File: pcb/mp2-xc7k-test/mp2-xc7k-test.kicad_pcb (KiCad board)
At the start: 4 copper layers, 0 parts

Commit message: Continued layout, 454 unrouted
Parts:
- added C1: 10 uF, azonenberg_pcb:EIA_1210_CAP_NOSILK, F.Cu at (95.0, 66.5)
- added C10: 0.47 uF, azonenberg_pcb:EIA_0402_CAP_NOSILK, F.Cu at (93.8, 99.2)
- added C100: 1 uF, azonenberg_pcb:EIA_0201_CAP_NOSILK, B.Cu at (200.0, 87.1)
- added C101: 1 uF, azonenberg_pcb:EIA_0201_CAP_NOSILK, B.Cu at (208.7, 92.0)
- added C102: 1 uF, azonenberg_pcb:EIA_0201_CAP_NOSILK, B.Cu at (205.6, 85.5)
- added C103: 1 uF, azonenberg_pcb:EIA_0201_CAP_NOSILK, B.Cu at (204.8, 83.3)
- added C104: 1 uF, azonenberg_pcb:EIA_0201_CAP_NOSILK, B.Cu at (199.2, 83.9)
- added C105: 1 uF, azonenberg_pcb:EIA_0201_CAP_NOSILK, B.Cu at (204.8, 84.7)
- added C106: 1 uF, azonenberg_pcb:EIA_0201_CAP_NOSILK, B.Cu at (201.5, 83.2)
- added C107: 1 uF, azonenberg_pcb:EIA_0201_CAP_NOSILK, B.Cu at (204.0, 85.5)
- added C108: 1 uF, azonenberg_pcb:EIA_0201_CAP_NOSILK, B.Cu at (199.2, 83.1)
- added C109: 1 uF, azonenberg_pcb:EIA_0201_CAP_NOSILK, B.Cu at (200.8, 85.5)
- added C11: DNP, azonenberg_pcb:EIA_0402_CAP_NOSILK, F.Cu at (93.8, 100.7)
- added C110: 1 uF, azonenberg_pcb:EIA_0201_CAP_NOSILK, B.Cu at (208.7, 91.2)
- added C111: 1 uF, azonenberg_pcb:EIA_0201_CAP_NOSILK, B.Cu at (207.2, 91.3)
- added C112: 1 uF, azonenberg_pcb:EIA_0201_CAP_NOSILK, B.Cu at (197.7, 80.8)
- added C113: 1 uF, azonenberg_pcb:EIA_0201_CAP_NOSILK, B.Cu at (197.6, 82.3)
- added C114: 1 uF, azonenberg_pcb:EIA_0201_CAP_NOSILK, B.Cu at (197.6, 83.0)
- added C115: 0.47 uF, azonenberg_pcb:EIA_0402_CAP_NOSILK, F.Cu at (98.8, 93.2)
- added C116: 0.47 uF, azonenberg_pcb:EIA_0402_CAP_NOSILK, F.Cu at (98.8, 94.7)
- added C117: 4.7 uF, azonenberg_pcb:EIA_0603_CAP_NOSILK, B.Cu at (197.2, 85.2)
- added C118: 1 uF, azonenberg_pcb:EIA_0201_CAP_NOSILK, B.Cu at (200.1, 80.8)
- added C119: 1 uF, azonenberg_pcb:EIA_0201_CAP_NOSILK, B.Cu at (200.1, 82.4)
- added C12: 22 uF, azonenberg_pcb:EIA_1210_CAP_NOSILK, F.Cu at (95.0, 70.4)
- added C120: 1 uF, azonenberg_pcb:EIA_0201_CAP_NOSILK, B.Cu at (198.5, 82.4)
- added C121: 1 uF, azonenberg_pcb:EIA_0201_CAP_NOSILK, B.Cu at (199.4, 80.8)
- added C122: 1 uF, azonenberg_pcb:EIA_0201_CAP_NOSILK, B.Cu at (198.5, 80.8)
- added C123: 4.7 uF, azonenberg_pcb:EIA_0603_CAP_NOSILK, B.Cu at (199.4, 91.6)
- added C124: DNP, azonenberg_pcb:EIA_0402_CAP_NOSILK, F.Cu at (98.8, 96.2)
- added C125: 4.7 uF, azonenberg_pcb:EIA_0603_CAP_NOSILK, F.Cu at (170.6, 147.0)
- added C126: 0.47 uF, azonenberg_pcb:EIA_0402_CAP_NOSILK, F.Cu at (144.7, 142.8)
- added C127: 0.47 uF, azonenberg_pcb:EIA_0402_CAP_NOSILK, F.Cu at (144.7, 144.3)
- added C128: 1 uF, azonenberg_pcb:EIA_0201_CAP_NOSILK, B.Cu at (197.6, 91.3)
- added C129: 22 uF, azonenberg_pcb:EIA_1210_CAP_NOSILK, F.Cu at (105.0, 66.5)
- added C13: 4.7 uF, azonenberg_pcb:EIA_0603_CAP_NOSILK, F.Cu at (88.8, 107.2)
- added C130: 0.47 uF, azonenberg_pcb:EIA_0402_CAP_NOSILK, F.Cu at (98.8, 97.7)
- added C131: 0.47 uF, azonenberg_pcb:EIA_0402_CAP_NOSILK, B.Cu at (196.8, 128.5)
- added C132: 0.47 uF, azonenberg_pcb:EIA_0402_CAP_NOSILK, B.Cu at (204.6, 103.2)
- added C133: 0.1 uF, azonenberg_pcb:EIA_0402_CAP_NOSILK, F.Cu at (205.2, 101.2)
- added C134: 0.1 uF, azonenberg_pcb:EIA_0402_CAP_NOSILK, F.Cu at (206.1, 101.2)
- added C135: 0.47 uF, azonenberg_pcb:EIA_0402_CAP_NOSILK, B.Cu at (201.6, 64.2)
- added C136: 4.7 uF, azonenberg_pcb:EIA_0603_CAP_NOSILK, F.Cu at (191.5, 63.2)
- added C137: 0.47 uF, azonenberg_pcb:EIA_0402_CAP_NOSILK, B.Cu at (195.1, 67.5)
- added C138: 0.47 uF, azonenberg_pcb:EIA_0402_CAP_NOSILK, B.Cu at (194.0, 63.6)
- added C139: 0.47 uF, azonenberg_pcb:EIA_0402_CAP_NOSILK, B.Cu at (199.0, 66.0)
- added C14: 4.7 uF, azonenberg_pcb:EIA_0603_CAP_NOSILK, F.Cu at (88.8, 109.0)
- added C140: 1 uF, azonenberg_pcb:EIA_0201_CAP_NOSILK, B.Cu at (198.3, 90.4)
- added C15: DNP, azonenberg_pcb:EIA_0402_CAP_NOSILK, F.Cu at (96.3, 88.7)
- added C16: 22 uF, azonenberg_pcb:EIA_1210_CAP_NOSILK, F.Cu at (95.0, 74.3)
- added C17: 0.47 uF, azonenberg_pcb:EIA_0402_CAP_NOSILK, F.Cu at (96.3, 90.2)
- added C18: 4.7 uF, azonenberg_pcb:EIA_0603_CAP_NOSILK, F.Cu at (88.8, 110.8)
- added C19: 4.7 uF, azonenberg_pcb:EIA_0603_CAP_NOSILK, F.Cu at (88.8, 112.7)
- added C2: 0.47 uF, azonenberg_pcb:EIA_0402_CAP_NOSILK, F.Cu at (93.8, 88.7)
- added C20: DNP, azonenberg_pcb:EIA_0402_CAP_NOSILK, F.Cu at (96.3, 91.7)
- added C21: 22 uF, azonenberg_pcb:EIA_1210_CAP_NOSILK, F.Cu at (95.0, 78.2)
- added C22: 0.47 uF, azonenberg_pcb:EIA_0402_CAP_NOSILK, F.Cu at (96.3, 93.2)
- added C23: 0.47 uF, azonenberg_pcb:EIA_0402_CAP_NOSILK, F.Cu at (96.3, 94.7)
- added C24: 10 uF, azonenberg_pcb:EIA_1210_CAP_NOSILK, F.Cu at (95.0, 82.1)
- added C25: 47 uF, azonenberg_pcb:EIA_1206_CAP_NOSILK, F.Cu at (112.5, 89.2)
- added C26: 47 uF, azonenberg_pcb:EIA_1206_CAP_NOSILK, F.Cu at (112.5, 91.8)
- added C267: 1 uF, azonenberg_pcb:EIA_0201_CAP_NOSILK, B.Cu at (196.9, 81.6)
- added C268: 1 uF, azonenberg_pcb:EIA_0201_CAP_NOSILK, B.Cu at (197.7, 78.4)
- added C269: 1 uF, azonenberg_pcb:EIA_0201_CAP_NOSILK, B.Cu at (206.3, 83.2)
- added C27: 0.47 uF, azonenberg_pcb:EIA_0402_CAP_NOSILK, F.Cu at (96.3, 96.2)
- added C270: 1 uF, azonenberg_pcb:EIA_0201_CAP_NOSILK, B.Cu at (207.2, 92.1)
- added C271: 1 uF, azonenberg_pcb:EIA_0201_CAP_NOSILK, B.Cu at (195.2, 78.5)
- added C272: 1 uF, azonenberg_pcb:EIA_0201_CAP_NOSILK, B.Cu at (207.2, 81.7)
- added C273: 1 uF, azonenberg_pcb:EIA_0201_CAP_NOSILK, B.Cu at (198.4, 84.6)
- added C274: 1 uF, azonenberg_pcb:EIA_0201_CAP_NOSILK, B.Cu at (199.2, 84.9)
- added C28: 10 uF, azonenberg_pcb:EIA_1210_CAP_NOSILK, F.Cu at (95.0, 86.0)
- added C29: 0.47 uF, azonenberg_pcb:EIA_0402_CAP_NOSILK, F.Cu at (96.3, 97.7)
- added C3: 4.7 uF, azonenberg_pcb:EIA_0603_CAP_NOSILK, F.Cu at (88.8, 105.5)
- added C30: 0.47 uF, azonenberg_pcb:EIA_0402_CAP_NOSILK, F.Cu at (96.3, 99.2)
- added C31: 10 uF, azonenberg_pcb:EIA_1210_CAP_NOSILK, F.Cu at (100.0, 66.5)
- added C32: 10 uF, azonenberg_pcb:EIA_1210_CAP_NOSILK, F.Cu at (100.0, 70.4)
- added C33: 22 uF, azonenberg_pcb:EIA_1206_CAP_NOSILK, F.Cu at (112.5, 94.4)
- added C34: 0.47 uF, azonenberg_pcb:EIA_0402_CAP_NOSILK, F.Cu at (96.3, 100.7)
- added C35: 10 uF, azonenberg_pcb:EIA_1210_CAP_NOSILK, F.Cu at (100.0, 74.3)
- added C36: 22 uF, azonenberg_pcb:EIA_1206_CAP_NOSILK, F.Cu at (112.5, 97.0)
- added C37: 0.47 uF, azonenberg_pcb:EIA_0402_CAP_NOSILK, F.Cu at (98.8, 88.7)
- added C38: 10 uF, azonenberg_pcb:EIA_1210_CAP_NOSILK, F.Cu at (100.0, 78.2)
- added C39: 47 uF, azonenberg_pcb:EIA_1206_CAP_NOSILK, F.Cu at (112.5, 99.6)
- added C4: 0.1 uF, azonenberg_pcb:EIA_0402_CAP_NOSILK, F.Cu at (93.8, 90.2)
- added C40: 0.47 uF, azonenberg_pcb:EIA_0402_CAP_NOSILK, F.Cu at (98.8, 90.2)
- added C41: 10 uF, azonenberg_pcb:EIA_1210_CAP_NOSILK, F.Cu at (100.0, 82.1)
- added C42: 0.47 uF, azonenberg_pcb:EIA_0402_CAP_NOSILK, F.Cu at (174.5, 149.5)
- added C43: 330 uF, azonenberg_pcb:EIA_1210_CAP_NOSILK, F.Cu at (127.8, 132.7)
- added C44: 0.22 uF, azonenberg_pcb:EIA_0402_CAP_NOSILK, F.Cu at (199.8, 107.0)
- added C45: 0.22 uF, azonenberg_pcb:EIA_0402_CAP_NOSILK, F.Cu at (199.8, 107.8)
- added C46: 0.22 uF, azonenberg_pcb:EIA_0402_CAP_NOSILK, F.Cu at (204.4, 109.6)
- added C47: 0.22 uF, azonenberg_pcb:EIA_0402_CAP_NOSILK, F.Cu at (204.4, 108.8)
- added C48: 22 uF, azonenberg_pcb:EIA_0805_CAP_NOSILK, F.Cu at (167.1, 143.2)
- added C49: 330 uF, azonenberg_pcb:EIA_1210_CAP_NOSILK, F.Cu at (127.8, 136.6)
- added C5: 0.47 uF, azonenberg_pcb:EIA_0402_CAP_NOSILK, F.Cu at (93.8, 91.7)
- added C50: 0.1 uF, azonenberg_pcb:EIA_0402_CAP_NOSILK, F.Cu at (142.2, 142.8)
- added C51: 0.1 uF, azonenberg_pcb:EIA_0402_CAP_NOSILK, F.Cu at (142.2, 144.3)
- added C52: 0.1 uF, azonenberg_pcb:EIA_0402_CAP_NOSILK, F.Cu at (199.8, 112.0)
- added C53: 0.1 uF, azonenberg_pcb:EIA_0402_CAP_NOSILK, F.Cu at (142.2, 147.3)
- added C54: 0.1 uF, azonenberg_pcb:EIA_0402_CAP_NOSILK, F.Cu at (144.7, 135.3)
- added C55: 22 uF, azonenberg_pcb:EIA_0805_CAP_NOSILK, F.Cu at (167.1, 145.8)
- added C56: 100 uF, azonenberg_pcb:EIA_1210_CAP_NOSILK, F.Cu at (127.8, 140.5)
- added C57: 4.7 uF, azonenberg_pcb:EIA_0603_CAP_NOSILK, F.Cu at (131.9, 131.7)
- added C58: 4.7 uF, azonenberg_pcb:EIA_0603_CAP_NOSILK, B.Cu at (175.0, 82.5)
- added C59: 4.7 uF, azonenberg_pcb:EIA_0603_CAP_NOSILK, B.Cu at (166.0, 82.5)
- added C6: 0.47 uF, azonenberg_pcb:EIA_0402_CAP_NOSILK, F.Cu at (93.8, 93.2)
- added C60: 47 uF, azonenberg_pcb:EIA_1210_CAP_NOSILK, F.Cu at (177.0, 98.4)
- added C61: 47 uF, azonenberg_pcb:EIA_1210_CAP_NOSILK, F.Cu at (177.0, 101.6)
- added C62: 47 uF, azonenberg_pcb:EIA_1210_CAP_NOSILK, F.Cu at (180.2, 104.8)
- added C63: 47 uF, azonenberg_pcb:EIA_1210_CAP_NOSILK, F.Cu at (121.2, 141.7)
- added C64: 4.7 uF, azonenberg_pcb:EIA_0603_CAP_NOSILK, F.Cu at (131.9, 137.1)
- added C65: 4.7 uF, azonenberg_pcb:EIA_0603_CAP_NOSILK, F.Cu at (131.9, 138.9)
- added C66: 4.7 uF, azonenberg_pcb:EIA_0603_CAP_NOSILK, F.Cu at (131.9, 140.7)
- added C67: 0.1 uF, azonenberg_pcb:EIA_0402_CAP_NOSILK, F.Cu at (199.8, 111.2)
- added C68: 0.47 uF, azonenberg_pcb:EIA_0402_CAP_NOSILK, B.Cu at (188.2, 93.0)
- added C69: 1 uF, azonenberg_pcb:EIA_0201_CAP_NOSILK, B.Cu at (200.8, 89.5)
- added C7: 0.47 uF, azonenberg_pcb:EIA_0402_CAP_NOSILK, F.Cu at (93.8, 94.7)
- added C70: 1 uF, azonenberg_pcb:EIA_0201_CAP_NOSILK, B.Cu at (200.8, 87.9)
- added C71: 1 uF, azonenberg_pcb:EIA_0201_CAP_NOSILK, B.Cu at (204.8, 89.5)
- added C72: 1 uF, azonenberg_pcb:EIA_0201_CAP_NOSILK, B.Cu at (203.2, 84.9)
- added C73: 1 uF, azonenberg_pcb:EIA_0201_CAP_NOSILK, B.Cu at (196.1, 80.0)
- added C74: 1 uF, azonenberg_pcb:EIA_0201_CAP_NOSILK, B.Cu at (200.8, 88.7)
- added C75: 0.47 uF, azonenberg_pcb:EIA_0402_CAP_NOSILK, F.Cu at (144.7, 138.3)
- added C76: 0.1 uF, azonenberg_pcb:EIA_0402_CAP_NOSILK, F.Cu at (144.7, 139.8)
- added C77: 0.1 uF, azonenberg_pcb:EIA_0402_CAP_NOSILK, F.Cu at (144.7, 141.3)
- added C78: 1 uF, azonenberg_pcb:EIA_0201_CAP_NOSILK, B.Cu at (203.2, 87.9)
- added C79: 1 uF, azonenberg_pcb:EIA_0201_CAP_NOSILK, B.Cu at (206.3, 89.6)
- added C8: 0.47 uF, azonenberg_pcb:EIA_0402_CAP_NOSILK, F.Cu at (93.8, 96.2)
- added C80: 1 uF, azonenberg_pcb:EIA_0201_CAP_NOSILK, B.Cu at (203.2, 84.1)
- added C81: 1 uF, azonenberg_pcb:EIA_0201_CAP_NOSILK, B.Cu at (200.8, 87.1)
- added C82: 1 uF, azonenberg_pcb:EIA_0201_CAP_NOSILK, B.Cu at (199.2, 89.5)
- added C83: 1 uF, azonenberg_pcb:EIA_0201_CAP_NOSILK, B.Cu at (203.2, 87.1)
- added C84: 1 uF, azonenberg_pcb:EIA_0201_CAP_NOSILK, B.Cu at (204.8, 88.7)
- added C85: 1 uF, azonenberg_pcb:EIA_0201_CAP_NOSILK, B.Cu at (203.2, 83.3)
- added C86: 1 uF, azonenberg_pcb:EIA_0201_CAP_NOSILK, B.Cu at (200.8, 84.7)
- added C87: 1 uF, azonenberg_pcb:EIA_0201_CAP_NOSILK, B.Cu at (199.2, 88.7)
- added C88: 1 uF, azonenberg_pcb:EIA_0201_CAP_NOSILK, B.Cu at (203.2, 88.7)
- added C89: 1 uF, azonenberg_pcb:EIA_0201_CAP_NOSILK, B.Cu at (204.8, 87.9)
- added C9: 0.47 uF, azonenberg_pcb:EIA_0402_CAP_NOSILK, F.Cu at (93.8, 97.7)
- added C90: 1 uF, azonenberg_pcb:EIA_0201_CAP_NOSILK, B.Cu at (203.2, 82.5)
- added C91: 1 uF, azonenberg_pcb:EIA_0201_CAP_NOSILK, B.Cu at (200.8, 83.9)
- added C92: 1 uF, azonenberg_pcb:EIA_0201_CAP_NOSILK, B.Cu at (199.2, 87.9)
- added C93: 1 uF, azonenberg_pcb:EIA_0201_CAP_NOSILK, B.Cu at (203.2, 89.5)
- added C94: 1 uF, azonenberg_pcb:EIA_0201_CAP_NOSILK, B.Cu at (204.8, 87.1)
- added C95: 22 uF, azonenberg_pcb:EIA_1206_CAP_NOSILK, F.Cu at (112.5, 102.2)
- added C96: 10 uF, azonenberg_pcb:EIA_1210_CAP_NOSILK, F.Cu at (100.0, 86.0)
- added C97: 0.47 uF, azonenberg_pcb:EIA_0402_CAP_NOSILK, F.Cu at (98.8, 91.7)
- added C98: 1 uF, azonenberg_pcb:EIA_0201_CAP_NOSILK, B.Cu at (204.8, 82.5)
- added C99: 1 uF, azonenberg_pcb:EIA_0201_CAP_NOSILK, B.Cu at (200.0, 84.7)
- added D1: GREEN, azonenberg_pcb:EIA_0402_LED, F.Cu at (98.8, 99.2)
- added D10: GREEN, azonenberg_pcb:EIA_0402_LED, F.Cu at (189.8, 82.8)
- added D11: GREEN, azonenberg_pcb:EIA_0402_LED, F.Cu at (190.5, 82.8)
- added D12: RED, azonenberg_pcb:EIA_0402_LED, F.Cu at (199.4, 122.0)
- added D2: GREEN, azonenberg_pcb:EIA_0402_LED, F.Cu at (98.8, 100.7)
- added D3: RED, azonenberg_pcb:EIA_0402_LED, F.Cu at (101.3, 88.7)
- added D31: GREEN, azonenberg_pcb:EIA_0402_LED, F.Cu at (154.2, 149.0)
- added D32: GREEN, azonenberg_pcb:EIA_0402_LED, F.Cu at (167.4, 133.8)
- added D33: GREEN, azonenberg_pcb:EIA_0402_LED, F.Cu at (167.4, 135.6)
- added D34: GREEN, azonenberg_pcb:EIA_0402_LED, F.Cu at (167.4, 137.3)
- added D39: GREEN, azonenberg_pcb:EIA_0402_LED, F.Cu at (167.4, 139.2)
- added D4: GREEN, azonenberg_pcb:EIA_0402_LED, F.Cu at (188.2, 79.5)
- added D40: GREEN, azonenberg_pcb:EIA_0402_LED, F.Cu at (167.4, 140.9)
- added D5: GREEN, azonenberg_pcb:EIA_0402_LED, F.Cu at (189.0, 79.5)
- added D6: GREEN, azonenberg_pcb:EIA_0402_LED, F.Cu at (189.8, 79.5)
- added D7: GREEN, azonenberg_pcb:EIA_0402_LED, F.Cu at (190.5, 79.5)
- added D8: GREEN, azonenberg_pcb:EIA_0402_LED, F.Cu at (188.2, 82.8)
- added D9: GREEN, azonenberg_pcb:EIA_0402_LED, F.Cu at (189.0, 82.8)
- added F1: 3A, azonenberg_pcb:EIA_0402_RES_NOSILK, F.Cu at (101.3, 90.2)
- added FB1: MI0603J601R-10, azonenberg_pcb:EIA_0603_INDUCTOR_NOSILK, F.Cu at (88.8, 114.5)
- added FB7: MI0603J601R-10, azonenberg_pcb:EIA_0603_INDUCTOR_NOSILK, B.Cu at (187.6, 90.6)
- added FB8: MI0603J601R-10, azonenberg_pcb:EIA_0603_INDUCTOR_NOSILK, B.Cu at (187.6, 91.6)
- added J1: BARREL_JACK, azonenberg_pcb:CONN_CUI_PJ-058BH_HIPWR_BARREL_NOSLOT, F.Cu at (131.5, 68.5)
- added J10: SMPM, azonenberg_pcb:CONN_SMPM_AMPHENOL_C925-197J-51PT, F.Cu at (196.0, 101.8)
- added J12: PMOD_HOST, azonenberg_pcb:CONN_HEADER_2.54MM_2x6_RA_PMOD_HOST, F.Cu at (188.3, 123.7)
- added J13: PMOD_HOST, azonenberg_pcb:CONN_HEADER_2.54MM_2x6_RA_PMOD_HOST, F.Cu at (169.8, 64.6)
- added J2: CORTEX_DEBUG_ETM, azonenberg_pcb:CONN_HEADER_1.27MM_2x10_SMT_SAMTEC_FTSH-110-01-L-DV-K, F.Cu at (135.0, 125.0)
- added J3: CONN_01X03, azonenberg_pcb:CONN_HEADER_2.54MM_1x3, F.Cu at (86.2, 93.9)
- added J4: CONN_SFP_HOST, azonenberg_pcb:CONN_SFP+_AMPHENOL_UE76_A10_2000T, F.Cu at (152.0, 109.5)
- added J5: CORTEX_DEBUG_ETM, azonenberg_pcb:CONN_HEADER_1.27MM_2x10_SMT_SAMTEC_FTSH-110-01-L-DV-K, F.Cu at (170.0, 125.0)
- added J6: XILINX_JTAG, azonenberg_pcb:XILINX_JTAG_PTH_MOLEX_0878311420, F.Cu at (153.0, 125.0)
- added J7: SFP_CAGE, azonenberg_pcb:CONN_SFP_CAGE_TE_2007194-1, F.Cu at (152.0, 109.5)
- added J8: CONN_01X06, azonenberg_pcb:CONN_HEADER_2.54MM_1x6_REFLOW, F.Cu at (204.8, 118.2)
- added L1: 2.2 uH, azonenberg_pcb:EIA_1210_CAP_NOSILK, F.Cu at (105.0, 70.4)
- added L2: 2.2 uH, azonenberg_pcb:EIA_1210_CAP_NOSILK, F.Cu at (105.0, 74.3)
- added L3: 2.2 uH, azonenberg_pcb:EIA_1210_CAP_NOSILK, F.Cu at (105.0, 78.2)
- added L4: 2.2 uH, azonenberg_pcb:EIA_1210_CAP_NOSILK, F.Cu at (105.0, 82.1)
- added L5: 2.2 uH, azonenberg_pcb:EIA_1210_CAP_NOSILK, F.Cu at (105.0, 86.0)
- added L6: 4.7 uH, azonenberg_pcb:EIA_0805_INDUCTOR_NOSILK, F.Cu at (167.1, 148.2)
- added L7: 4.7 uH, azonenberg_pcb:EIA_0805_INDUCTOR_NOSILK, F.Cu at (167.1, 150.3)
- added M1: 960-27-12-F-AB-0, azonenberg_pcb:HEATSINK_WAKEFIELDVETTE_960-27-12-D-AB-0, F.Cu at (170.5, 82.5)
- added M10: SCREWHOLE, azonenberg_pcb:MECHANICAL_CLEARANCEHOLE_4_40, F.Cu at (212.0, 125.0)
- added M2: SCREWHOLE, azonenberg_pcb:MECHANICAL_CLEARANCEHOLE_4_40, F.Cu at (122.0, 125.0)
- added M3: SCREWHOLE, azonenberg_pcb:MECHANICAL_CLEARANCEHOLE_4_40, F.Cu at (122.0, 65.0)
- added M4: SCREWHOLE, azonenberg_pcb:MECHANICAL_CLEARANCEHOLE_4_40, F.Cu at (212.0, 65.0)
- added M5: LOGO_LONGTHING, azonenberg_pcb:LONGTHING-1200DPI, F.Cu at (183.6, 64.6)
- added M6: LOGO_ESD, azonenberg_pcb:LOGO_ESD_SENSITIVE_7MM, F.Cu at (213.4, 72.4)
- added M7: LOGO_OSHW, w_logo:Logo_silk_OSHW_6x6mm, F.Cu at (214.2, 88.4)
- added M8: LOGO_ROHS, w_logo:Logo_silk_ROHS_5x2.8mm, F.Cu at (214.0, 84.4)
- added M9: LOGO_WEEE, w_logo:Logo_silk_WEEE_3.4x5mm, F.Cu at (214.0, 79.2)
- added R1: 10K, azonenberg_pcb:EIA_0402_RES_NOSILK, F.Cu at (101.3, 91.7)
- added R10: 33, azonenberg_pcb:EIA_0402_RES_NOSILK, B.Cu at (170.7, 91.0)
- added R11: 4.7K, azonenberg_pcb:EIA_0402_RES_NOSILK, F.Cu at (103.8, 91.7)
- added R12: 162K, azonenberg_pcb:EIA_0402_RES_NOSILK, F.Cu at (103.8, 93.2)
- added R124: 1K, azonenberg_pcb:EIA_0402_RES_NOSILK, F.Cu at (149.7, 138.3)
- added R126: 33, azonenberg_pcb:EIA_0402_RES_NOSILK, F.Cu at (149.7, 139.8)
- added R127: 33, azonenberg_pcb:EIA_0402_RES_NOSILK, F.Cu at (149.7, 141.3)
- added R128: 33, azonenberg_pcb:EIA_0402_RES_NOSILK, F.Cu at (149.7, 142.8)
- added R129: 33, azonenberg_pcb:EIA_0402_RES_NOSILK, F.Cu at (149.7, 144.3)
- added R13: 511K, azonenberg_pcb:EIA_0402_RES_NOSILK, F.Cu at (103.8, 94.7)
- added R14: 10K, azonenberg_pcb:EIA_0402_RES_NOSILK, F.Cu at (103.8, 96.2)
- added R15: 255K, azonenberg_pcb:EIA_0402_RES_NOSILK, F.Cu at (103.8, 97.7)
- added R157: 33K, azonenberg_pcb:EIA_0402_RES_NOSILK, F.Cu at (149.7, 145.8)
- added R158: 33K, azonenberg_pcb:EIA_0402_RES_NOSILK, F.Cu at (149.7, 147.3)
- added R159: 33K, azonenberg_pcb:EIA_0402_RES_NOSILK, F.Cu at (152.2, 135.3)
- added R16: 1.02M, azonenberg_pcb:EIA_0402_RES_NOSILK, F.Cu at (103.8, 99.2)
- added R160: 33K, azonenberg_pcb:EIA_0402_RES_NOSILK, F.Cu at (152.2, 136.8)
- added R161: 1K, azonenberg_pcb:EIA_0402_RES_NOSILK, F.Cu at (152.2, 138.3)
- added R162: 1K, azonenberg_pcb:EIA_0402_RES_NOSILK, F.Cu at (152.2, 139.8)
- added R163: 33K, azonenberg_pcb:EIA_0402_RES_NOSILK, F.Cu at (152.2, 141.3)
- added R164: 33K, azonenberg_pcb:EIA_0402_RES_NOSILK, F.Cu at (152.2, 142.8)
- added R165: 4.7K, azonenberg_pcb:EIA_0402_RES_NOSILK, F.Cu at (152.2, 144.3)
- added R17: 255K, azonenberg_pcb:EIA_0402_RES_NOSILK, F.Cu at (103.8, 100.7)
- added R18: 1.02M, azonenberg_pcb:EIA_0402_RES_NOSILK, F.Cu at (106.3, 88.7)
- added R19: 24.9K, azonenberg_pcb:EIA_0402_RES_NOSILK, F.Cu at (106.3, 90.2)
- added R2: 33, azonenberg_pcb:EIA_0402_RES_NOSILK, F.Cu at (101.3, 93.2)
- added R20: 200K, azonenberg_pcb:EIA_0402_RES_NOSILK, F.Cu at (106.3, 91.7)
- added R21: 24.9K, azonenberg_pcb:EIA_0402_RES_NOSILK, F.Cu at (106.3, 93.2)
- added R22: 1M, azonenberg_pcb:EIA_0402_RES_NOSILK, F.Cu at (106.3, 94.7)
- added R23: 10K, azonenberg_pcb:EIA_0402_RES_NOSILK, F.Cu at (106.3, 96.2)
- added R24: 10K, azonenberg_pcb:EIA_0402_RES_NOSILK, F.Cu at (106.3, 97.7)
- added R25: 10K, azonenberg_pcb:EIA_0402_RES_NOSILK, F.Cu at (106.3, 99.2)
- added R26: 10K, azonenberg_pcb:EIA_0402_RES_NOSILK, F.Cu at (106.3, 100.7)
- added R27: 10K, azonenberg_pcb:EIA_0402_RES_NOSILK, F.Cu at (108.8, 88.7)
- added R28: 10K, azonenberg_pcb:EIA_0402_RES_NOSILK, F.Cu at (108.8, 90.2)
- added R29: 10K, azonenberg_pcb:EIA_0402_RES_NOSILK, F.Cu at (108.8, 91.7)
- added R3: 0, azonenberg_pcb:EIA_0402_RES_NOSILK, F.Cu at (101.3, 94.7)
- added R30: 33, azonenberg_pcb:EIA_0402_RES_NOSILK, F.Cu at (144.7, 145.8)
- added R31: 33, azonenberg_pcb:EIA_0402_RES_NOSILK, B.Cu at (158.5, 87.5)
- added R32: 33, azonenberg_pcb:EIA_0402_RES_NOSILK, F.Cu at (144.7, 147.3)
- added R33: 33, azonenberg_pcb:EIA_0402_RES_NOSILK, F.Cu at (147.2, 135.3)
- added R34: 33, azonenberg_pcb:EIA_0402_RES_NOSILK, F.Cu at (147.2, 136.8)
- added R35: 100, azonenberg_pcb:EIA_0402_RES_NOSILK, B.Cu at (169.0, 91.5)
- added R36: 33, azonenberg_pcb:EIA_0402_RES_NOSILK, F.Cu at (147.2, 139.8)
- added R37: 33, azonenberg_pcb:EIA_0402_RES_NOSILK, F.Cu at (147.2, 141.3)
- added R38: 10K, azonenberg_pcb:EIA_0402_RES_NOSILK, F.Cu at (147.2, 142.8)
- added R39: 33, azonenberg_pcb:EIA_0402_RES_NOSILK, B.Cu at (190.6, 91.6)
- added R4: 4.7K, azonenberg_pcb:EIA_0402_RES_NOSILK, F.Cu at (101.3, 96.2)
- added R40: DNP, azonenberg_pcb:EIA_0402_RES_NOSILK, B.Cu at (196.8, 94.1)
- added R41: 10K, azonenberg_pcb:EIA_0402_RES_NOSILK, B.Cu at (194.0, 95.0)
- added R42: 10K, azonenberg_pcb:EIA_0402_RES_NOSILK, B.Cu at (165.4, 120.4)
- added R43: 33, azonenberg_pcb:EIA_0402_RES_NOSILK, B.Cu at (192.2, 92.4)
- added R44: 33K, azonenberg_pcb:EIA_0402_RES_NOSILK, F.Cu at (108.8, 93.2)
- added R45: 1K, azonenberg_pcb:EIA_0402_RES_NOSILK, B.Cu at (193.0, 90.8)
- added R46: 10K, azonenberg_pcb:EIA_0402_RES_NOSILK, F.Cu at (108.8, 94.7)
- added R47: 10K, azonenberg_pcb:EIA_0402_RES_NOSILK, F.Cu at (108.8, 96.2)
- added R48: 0.1, azonenberg_pcb:EIA_0402_RES_NOSILK, F.Cu at (147.2, 144.3)
- added R49: 0.5, azonenberg_pcb:EIA_0402_RES_NOSILK, F.Cu at (147.2, 145.8)
- added R5: 4.7K, azonenberg_pcb:EIA_0402_RES_NOSILK, F.Cu at (101.3, 97.7)
- added R50: 0.5, azonenberg_pcb:EIA_0402_RES_NOSILK, F.Cu at (147.2, 147.3)
- added R51: 4.7K, azonenberg_pcb:EIA_0402_RES_NOSILK, F.Cu at (149.7, 135.3)
- added R52: 4.7K, azonenberg_pcb:EIA_0402_RES_NOSILK, F.Cu at (149.7, 136.8)
- added R53: 10K, azonenberg_pcb:EIA_0402_RES_NOSILK, F.Cu at (108.8, 97.7)
- added R54: 33K, azonenberg_pcb:EIA_0402_RES_NOSILK, F.Cu at (188.2, 77.5)
- added R55: 33K, azonenberg_pcb:EIA_0402_RES_NOSILK, F.Cu at (189.0, 77.5)
- added R56: 33K, azonenberg_pcb:EIA_0402_RES_NOSILK, F.Cu at (189.8, 77.5)
- added R57: 33K, azonenberg_pcb:EIA_0402_RES_NOSILK, F.Cu at (190.5, 77.5)
- added R58: 4.7K, azonenberg_pcb:EIA_0402_RES_NOSILK, B.Cu at (190.1, 127.5)
- added R59: 4.7K, azonenberg_pcb:EIA_0402_RES_NOSILK, B.Cu at (190.1, 128.7)
- added R6: DNP, azonenberg_pcb:EIA_0402_RES_NOSILK, F.Cu at (101.3, 99.2)
- added R60: 33, azonenberg_pcb:EIA_0402_RES_NOSILK, B.Cu at (203.5, 69.8)
- added R61: 33, azonenberg_pcb:EIA_0402_RES_NOSILK, B.Cu at (204.8, 69.8)
- added R62: 33, azonenberg_pcb:EIA_0402_RES_NOSILK, B.Cu at (203.2, 64.9)
- added R63: 33, azonenberg_pcb:EIA_0402_RES_NOSILK, B.Cu at (205.9, 64.9)
- added R64: 10K, azonenberg_pcb:EIA_0402_RES_NOSILK, B.Cu at (201.5, 69.2)
- added R65: 10K, azonenberg_pcb:EIA_0402_RES_NOSILK, B.Cu at (205.5, 71.5)
- added R66: 10K, azonenberg_pcb:EIA_0402_RES_NOSILK, B.Cu at (202.5, 64.9)
- added R67: 33, azonenberg_pcb:EIA_0402_RES_NOSILK, B.Cu at (208.8, 76.0)
- added R68: 33, azonenberg_pcb:EIA_0402_RES_NOSILK, B.Cu at (207.2, 76.0)
- added R69: 33, azonenberg_pcb:EIA_0402_RES_NOSILK, B.Cu at (208.0, 76.0)
- added R7: 10K, azonenberg_pcb:EIA_0402_RES_NOSILK, F.Cu at (101.3, 100.7)
- added R70: 33, azonenberg_pcb:EIA_0402_RES_NOSILK, B.Cu at (205.6, 76.0)
- added R71: 33, azonenberg_pcb:EIA_0402_RES_NOSILK, B.Cu at (206.4, 76.0)
- added R72: 33, azonenberg_pcb:EIA_0402_RES_NOSILK, B.Cu at (200.8, 76.0)
- added R73: 33, azonenberg_pcb:EIA_0402_RES_NOSILK, B.Cu at (203.2, 76.0)
- added R74: 33, azonenberg_pcb:EIA_0402_RES_NOSILK, B.Cu at (202.4, 76.0)
- added R75: 33, azonenberg_pcb:EIA_0402_RES_NOSILK, B.Cu at (204.0, 76.0)
- added R76: 33, azonenberg_pcb:EIA_0402_RES_NOSILK, B.Cu at (204.8, 76.0)
- added R77: 33, azonenberg_pcb:EIA_0402_RES_NOSILK, B.Cu at (201.6, 76.0)
- added R78: 33K, azonenberg_pcb:EIA_0402_RES_NOSILK, F.Cu at (188.2, 84.8)
- added R79: 33K, azonenberg_pcb:EIA_0402_RES_NOSILK, F.Cu at (189.0, 84.8)
- added R8: 10K, azonenberg_pcb:EIA_0402_RES_NOSILK, F.Cu at (103.8, 88.7)
- added R80: 33K, azonenberg_pcb:EIA_0402_RES_NOSILK, F.Cu at (189.8, 84.8)
- added R81: 33K, azonenberg_pcb:EIA_0402_RES_NOSILK, F.Cu at (190.5, 84.8)
- added R82: 33, azonenberg_pcb:EIA_0402_RES_NOSILK, F.Cu at (199.6, 97.2)
- added R83: DNP, azonenberg_pcb:EIA_0402_RES_NOSILK, B.Cu at (197.5, 67.5)
- added R84: 10K, azonenberg_pcb:EIA_0402_RES_NOSILK, B.Cu at (195.6, 72.4)
- added R85: 4.7K, azonenberg_pcb:EIA_0402_RES_NOSILK, B.Cu at (199.0, 119.6)
- added R86: 33, azonenberg_pcb:EIA_0402_RES_NOSILK, B.Cu at (203.6, 116.2)
- added R87: 33, azonenberg_pcb:EIA_0402_RES_NOSILK, B.Cu at (201.0, 116.2)
- added R88: 33, azonenberg_pcb:EIA_0402_RES_NOSILK, F.Cu at (201.6, 75.6)
- added R89: 33, azonenberg_pcb:EIA_0402_RES_NOSILK, F.Cu at (202.4, 75.6)
- added R9: 33K, azonenberg_pcb:EIA_0402_RES_NOSILK, F.Cu at (103.8, 90.2)
- added R90: 100, azonenberg_pcb:EIA_0402_RES_NOSILK, B.Cu at (210.2, 93.2)
- added R91: 100, azonenberg_pcb:EIA_0402_RES_NOSILK, B.Cu at (210.7, 91.9)
- added SW1: SWITCH, azonenberg_pcb:SWITCH_RAFI_MICON_5, F.Cu at (139.5, 64.5)
- added SW2: SWITCH, azonenberg_pcb:SWITCH_RAFI_MICON_5, F.Cu at (145.5, 64.5)
- added TP1: U.FL, azonenberg_pcb:CONN_U.FL_TE_1909763-1, F.Cu at (84.2, 67.1)
- added TP10: CONN_01X03, azonenberg_pcb:CONN_HEADER_2.54MM_1x3, F.Cu at (86.2, 99.0)
- added TP11: U.FL, azonenberg_pcb:CONN_U.FL_TE_1909763-1, F.Cu at (190.0, 73.2)
- added TP12: U.FL, azonenberg_pcb:CONN_U.FL_TE_1909763-1, F.Cu at (89.8, 88.5)
- added TP2: U.FL, azonenberg_pcb:CONN_U.FL_TE_1909763-1, F.Cu at (84.2, 72.5)
- added TP3: U.FL, azonenberg_pcb:CONN_U.FL_TE_1909763-1, F.Cu at (84.2, 77.8)
- added TP4: U.FL, azonenberg_pcb:CONN_U.FL_TE_1909763-1, F.Cu at (84.2, 83.2)
- added TP5: U.FL, azonenberg_pcb:CONN_U.FL_TE_1909763-1, F.Cu at (84.2, 88.5)
- added TP6: U.FL, azonenberg_pcb:CONN_U.FL_TE_1909763-1, F.Cu at (89.8, 67.1)
- added TP7: U.FL, azonenberg_pcb:CONN_U.FL_TE_1909763-1, F.Cu at (89.8, 72.5)
- added TP8: U.FL, azonenberg_pcb:CONN_U.FL_TE_1909763-1, F.Cu at (89.8, 77.8)
- added TP9: U.FL, azonenberg_pcb:CONN_U.FL_TE_1909763-1, F.Cu at (89.8, 83.2)
- added U1: LTC3374-QFN, azonenberg_pcb:QFN_38_0.5MM_5x7MM, F.Cu at (126.2, 85.2)
- added U10: SIT9121AI-2BF-XXS156.250000G, azonenberg_pcb:OSCILLATOR_LVDS_3.2x2.5, F.Cu at (171.2, 143.8)
- added U11: ECS-1612MV-250-CN, azonenberg_pcb:OSCILLATOR_1.6x1.2, F.Cu at (170.5, 149.0)
- added U12: ECS-1612MV-250-CN, azonenberg_pcb:OSCILLATOR_1.6x1.2, B.Cu at (189.6, 93.0)
- added U13: TCA6424A, azonenberg_pcb:QFN_32_0.5MM_5x5MM, F.Cu at (142.9, 83.1)
- added U14: NCP45525IMNTWG-H, azonenberg_pcb:DFN_8_0.5MM_2x2MM, F.Cu at (85.4, 115.0)
- added U15: AT24MAC402, azonenberg_pcb:DFN_8_0.5MM_2x3MM_TALL, F.Cu at (199.8, 127.8)
- added U16: SIT9121AI-2BF-XXS200.000000G, azonenberg_pcb:OSCILLATOR_LVDS_3.2x2.5, F.Cu at (205.2, 104.2)
- added U17: W25Q80BV, azonenberg_pcb:SOIC_8_5.3MM, F.Cu at (204.0, 66.2)
- added U18: S27KL0642GABHB020, azonenberg_pcb:BGA_24_6x8_DEPOP1_1MM, F.Cu at (196.0, 66.5)
- added U2: STM32L431-QFN48, azonenberg_pcb:QFN_48_0.5MM_7x7MM, F.Cu at (139.5, 93.5)
- added U3: NCP45525IMNTWG-H, azonenberg_pcb:DFN_8_0.5MM_2x2MM, F.Cu at (85.4, 106.1)
- added U32: S25FL128SAGBHIA10, azonenberg_pcb:BGA_24_6x8_DEPOP1_1MM, F.Cu at (157.5, 139.7)
- added U4: XC7K160T-1FFG676C, azonenberg_pcb:BGA_676_27x27_FULLARRAY_1MM_FFG676, F.Cu at (170.5, 82.5)
- added U5: STM32MP257FAI3, azonenberg_pcb:BGA_436_18x18_DEPOP_0.8MM, F.Cu at (202.0, 86.0)
- added U6: LDO1117-18, azonenberg_pcb:SOT223-4, F.Cu at (96.3, 106.2)
- added U7: NCP45525IMNTWG-H, azonenberg_pcb:DFN_8_0.5MM_2x2MM, F.Cu at (85.4, 109.1)
- added U8: LDO1117-12, azonenberg_pcb:SOT223-4, F.Cu at (104.0, 106.2)
- added U9: NCP45525IMNTWG-H, azonenberg_pcb:DFN_8_0.5MM_2x2MM, F.Cu at (85.4, 112.0)
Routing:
- net /GND: track 0.00 -> 917.8 mm, vias 0 -> 266
- net /3V3: track 0.00 -> 559.4 mm, vias 0 -> 67
- net /1V8: track 0.00 -> 164.7 mm, vias 0 -> 31
- net /1V2: track 0.00 -> 130.1 mm, vias 0 -> 16
- net /SoC support/SOC_RST_N: track 0.00 -> 110.5 mm, vias 0 -> 3
- net /0V82: track 0.00 -> 108.4 mm, vias 0 -> 19
- net /SoC support/TRACED2: track 0.00 -> 93.9 mm, vias 0 -> 1
- net /SoC support/TRACED0: track 0.00 -> 90.9 mm, vias 0 -> 1
- net /SoC support/TRACED3: track 0.00 -> 90.1 mm, vias 0 -> 1
- net /SoC support/TRACED1: track 0.00 -> 87.5 mm, vias 0 -> 1
- net /SoC support/TRACECLK: track 0.00 -> 86.9 mm, vias 0 -> 1
- net /0V9: track 0.00 -> 85.9 mm, vias 0 -> 7
- net /1V8_2: track 0.00 -> 77.5 mm, vias 0 -> 3
- net /SoC support/A1V8: track 0.00 -> 63.0 mm, vias 0 -> 11
- net /SoC/I2C_SDA: track 0.00 -> 57.9 mm, vias 0 -> 3
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- added copper zone on F.Cu, net /GND
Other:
- board outline added: 100 x 70 mm
- board text added: "+"
- board text added: "0"
- board text added: "1"
- board text added: "2"
- board text added: "3"
- board text added: "3V3"
- board text added: "4 0"
- board text added: "5 1"
- board text added: "6 2"
- board text added: "7 3"
- board text added: "FPGA DEBUG"
- board text added: "GND"
- board text added: "LPUART_RX"
- board text added: "LPUART_TX"
- board text added: "LP_LED"
- board text added: "MCO1"
- board text added: "PCIE REF"
- board text added: "PCIE RX"
- board text added: "PCIE TX"
- board text added: "RX"
- board text added: "SOC DEBUG"
- board text added: "SOC LED"
- board text added: "SOC PMOD"
- board text added: "SUPER DEBUG"
- board text added: "TX"
- board text added: "~{BOOTFAIL}"

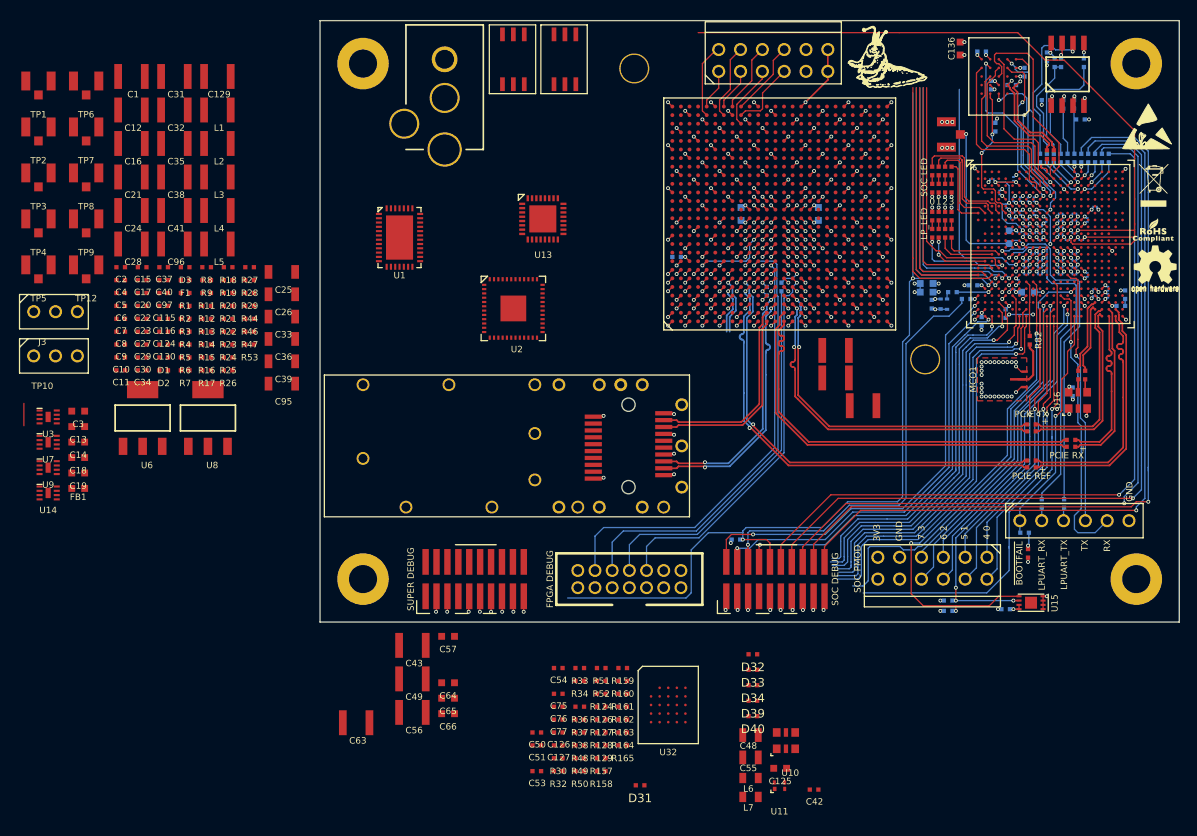
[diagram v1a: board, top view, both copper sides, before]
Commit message: Continued PCB routing, 344 nets left
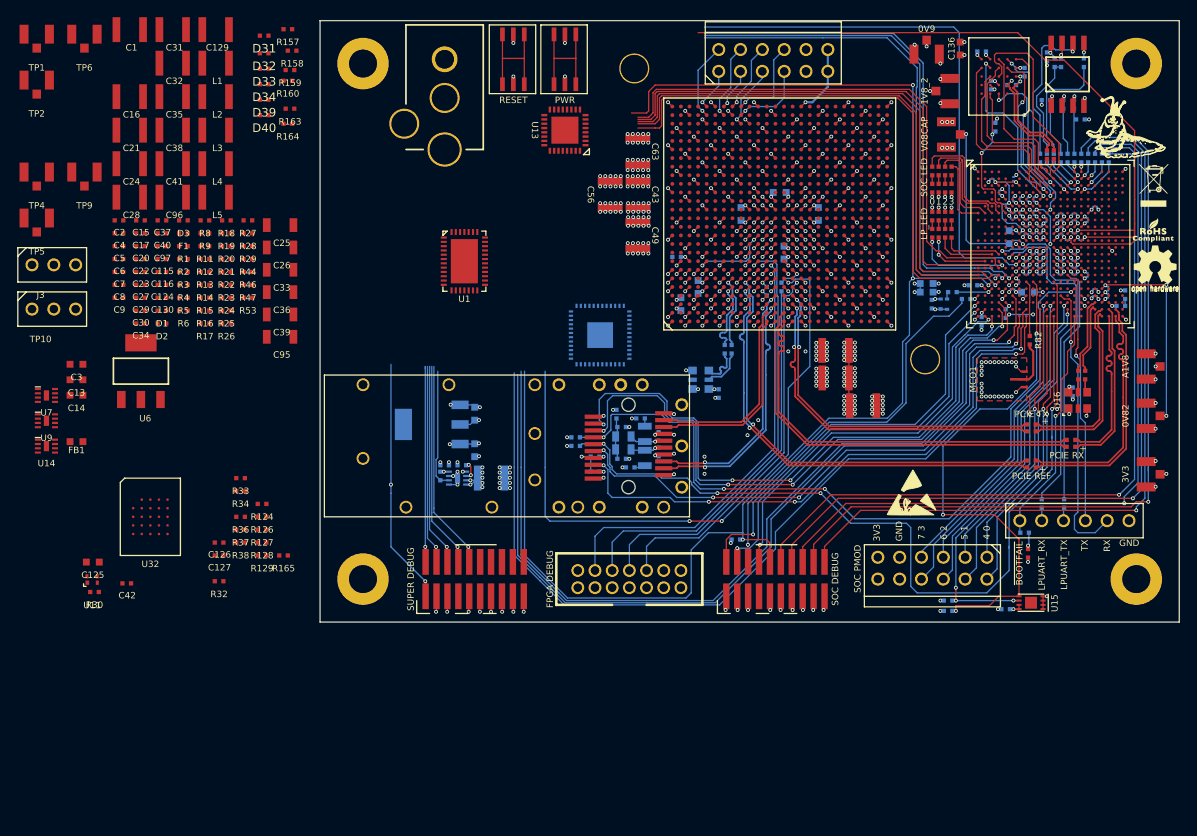
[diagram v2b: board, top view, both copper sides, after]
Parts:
- added TP13: U.FL, azonenberg_pcb:CONN_U.FL_TE_1909763-1, F.Cu at (213.2, 100.2)
- C10, C11, C12, C18, C19, C48, C50, C51, C53, C54, C55, C57, C64, C65, C66, C75, C76, C77, L6, L7, R161, R162, R48, R49, R50, R51, R52, R7, U10, U2, U3, U8: moved to B.Cu
- moved TP3 133.7 mm to (213.2, 112.8), turned to 90 degrees
- moved TP8 126.6 mm to (213.2, 106.0), turned to 90 degrees
- moved TP12 102.5 mm to (190.2, 68.2), turned to -90 degrees
- moved TP7 98.2 mm to (187.6, 63.8), turned to 180 degrees
- moved D31 97.6 mm to (110.5, 61.8)
- moved R157 92.4 mm to (113.2, 61.0)
- moved R158 91.2 mm to (113.8, 63.5)
- moved D33 90.2 mm to (110.5, 65.6)
- moved D32 90.2 mm to (110.5, 63.8)
- moved D34 90.2 mm to (110.5, 67.4)
- moved D39 90.2 mm to (110.5, 69.2)
- moved D40 90.2 mm to (110.5, 71.0)
- moved C125 83.5 mm to (90.5, 123.0)
- moved C42 83.5 mm to (94.5, 125.5)
- moved U11 83.5 mm to (90.5, 125.0)
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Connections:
- U10 pad 4: /FPGA/GTX1_REF_AC_P -> /FPGA/GTX1_REF_AC_N
- U10 pad 5: /FPGA/GTX1_REF_AC_N -> /FPGA/GTX1_REF_AC_P
- U5 pad AA4: /Power supply/SOC_READY -> /FPGA/SFP_TX_DISABLE
- U5 pad AA8: /FPGA/SFP_MOD_ABS -> /FPGA/SFP_RX_LOS
- U5 pad AB3: /FPGA/SFP_TX_DISABLE -> /FPGA/SFP_TX_FAULT
- U5 pad AB7: /FPGA/SFP_RX_LOS -> /FPGA/SFP_MOD_ABS
- U5 pad AB8: /FPGA/SFP_TX_FAULT -> /Power supply/SOC_READY
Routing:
- net /GND: track 917.8 -> 1246.3 mm, vias 266 -> 376
- net /3V3: track 559.4 -> 668.8 mm, vias 67 -> 92
- net /3V3_RAW: track 26.7 -> 134.3 mm, vias 1 -> 13
- net /FPGA support/FPGA_PROG_B: track 0.71 -> 73.4 mm, vias 1 -> 3
- net /Power supply/SOC_READY: track 43.7 -> 104.1 mm
- net /SoC support/SOC_RST_N: track 110.5 -> 170.7 mm, vias 3 -> 4
- net /Power supply/SUPER_I2C_SCL: track 47.0 -> 104.3 mm
- net /Power supply/SUPER_I2C_SDA: track 45.3 -> 102.3 mm
- net /1V8: track 164.7 -> 211.7 mm, vias 31 -> 61
- net /FPGA/SFP_I2C_SCL: track 54.5 -> 101.3 mm, vias 1 -> 4
- net /FPGA/SFP_I2C_SDA: track 51.5 -> 89.8 mm, vias 1 -> 4
- net /Power supply/SOC_BOOT0: track 27.9 -> 62.9 mm
- net /Power supply/SOC_BOOT1: track 28.5 -> 62.9 mm
- net /Power supply/SOC_BOOT2: track 28.9 -> 62.7 mm
- net /Power supply/SOC_BOOT3: track 28.6 -> 61.7 mm
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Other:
- board text added: "0V82"
- board text added: "0V9"
- board text added: "1V8_2"
- board text added: "A1V8"
- board text added: "PWR"
- board text added: "RESET"
- board text added: "V08CAP"

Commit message: 111 unrouted, getting close
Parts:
- removed C28, C41: 10 uF, azonenberg_pcb:EIA_1210_CAP_NOSILK
- removed R27: 10K, azonenberg_pcb:EIA_0402_RES_NOSILK
- C1, C115, C116, C125, C126, C127, C20, C21, C22, C31, C35, C4, C42, C5, C6, C7, C8, C9, C95, R1, R124, R126, R127, R128, R129, R14, R165, R28, R30, R32, R33, R34, R36, R37, R38, R4, R46, R47, R5, R53, R6, U11, U9: moved to B.Cu
- C24: value 10 uF -> 22 uF; moved to B.Cu
- C38: value 10 uF -> 22 uF
- TP10: value CONN_01X03 -> CONN_01X05; footprint azonenberg_pcb:CONN_HEADER_2.54MM_1x3 -> azonenberg_pcb:CONN_HEADER_2.54MM_1x5_REFLOW
- U2: moved to F.Cu
- moved R30 88.8 mm to (163.5, 75.5), turned to -90 degrees
- moved U11 88.7 mm to (164.8, 76.5), turned to 180 degrees
- moved C42 85.0 mm to (164.7, 77.6), turned to 180 degrees
- moved TP5 81.5 mm to (163.5, 101.0), turned to 180 degrees
- moved TP2 77.6 mm to (155.0, 98.5), turned to -90 degrees
- moved R32 76.4 mm to (160.5, 72.5), turned to 180 degrees
- moved D40 72.8 mm to (183.0, 64.2), turned to -90 degrees
- moved D39 71.9 mm to (182.2, 64.2), turned to -90 degrees
- moved D34 70.3 mm to (180.8, 64.2), turned to -90 degrees
- moved R38 70.0 mm to (158.0, 72.0), turned to 90 degrees
- moved R164 70.0 mm to (183.0, 66.0), turned to 90 degrees
- moved D33 69.5 mm to (180.0, 64.2), turned to -90 degrees
- moved C125 69.5 mm to (143.2, 77.8), turned to 180 degrees
- moved R163 68.9 mm to (182.2, 66.0), turned to 90 degrees
- moved R37 68.8 mm to (160.0, 74.5), turned to 90 degrees
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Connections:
- C27 pad 1: Net-(C27-Pad1) -> /Power supply/5V0
- C27 pad 2: Net-(C27-Pad2) -> /GND
- C29 pad 1: Net-(C29-Pad1) -> /Power supply/5V0
- C29 pad 2: Net-(C29-Pad2) -> /GND
- C31 pad 1: Net-(C29-Pad1) -> /Power supply/5V0
- C31 pad 2: Net-(C29-Pad2) -> /GND
- L2 pad 1: /3V3_RAW -> Net-(U1A-SW1)
- L2 pad 2: Net-(U1A-SW1) -> /3V3_RAW
- U13 pad 1: /Power supply/SOC_BOOT0 -> unconnected-(U13-P00-Pad1)
- U13 pad 10: unconnected-(U13-P11-Pad10) -> /Power supply/SOC_PWR_ON
- U13 pad 11: unconnected-(U13-P12-Pad11) -> /Power supply/SOC_PWR_CPU_ON
- U13 pad 15: unconnected-(U13-P16-Pad15) -> /Power supply/SOFT_POWER
- U13 pad 16: unconnected-(U13-P17-Pad16) -> /Power supply/SOFT_RESET
- U13 pad 18: /Power supply/SUPER_FAULT_LED -> unconnected-(U13-P21-Pad18)
- U13 pad 2: /Power supply/SOC_BOOT1 -> unconnected-(U13-P01-Pad2)
- U13 pad 21: unconnected-(U13-P24-Pad21) -> /Power supply/SUPER_FAULT_LED
- U13 pad 3: /Power supply/SOC_BOOT2 -> /Power supply/SOC_NRST1CMS
- U13 pad 5: /Power supply/SOC_NRST1CMS -> /Power supply/SOC_BOOT2
- U13 pad 6: unconnected-(U13-P05-Pad6) -> /Power supply/SOC_BOOT1
- U13 pad 7: unconnected-(U13-P06-Pad7) -> /Power supply/SOC_BOOT0
- U13 pad 8: unconnected-(U13-P07-Pad8) -> /SoC support/SOC_RST_N
- U13 pad 9: unconnected-(U13-P10-Pad9) -> /Power supply/SOC_PWR_LP
- U2 pad 10: /3V3 -> /1V8_2
- U2 pad 11: /1V8 -> /3V3
- U2 pad 12: /1V2 -> /Power supply/LTC_VTEMP
- U2 pad 16: /Power supply/LTC_VTEMP -> /1V2
- U2 pad 17: /FPGA support/GTX_1V0 -> /1V8
- U2 pad 18: /1V8_2 -> /FPGA support/GTX_1V0
- U2 pad 2: /FPGA support/FPGA_DONE -> /Power supply/GTX_1V0_EN
- U2 pad 20: /Power supply/SOC_PWR_ON -> unconnected-(U2B-PB2-Pad20)
- U2 pad 21: /FPGA support/FPGA_PROG_B -> /FPGA support/FPGA_DONE
- U2 pad 25: /Power supply/SOFT_POWER -> unconnected-(U2B-PB12-Pad25)
- U2 pad 28: /Power supply/SOFT_RESET -> unconnected-(U2B-PB15-Pad28)
- U2 pad 3: /Power supply/SOC_PWR_CPU_ON -> unconnected-(U2C-PC14-Pad3)
- U2 pad 4: /Power supply/SOC_PWR_LP -> unconnected-(U2C-PC15-Pad4)
- U2 pad 45: /SoC support/SOC_RST_N -> unconnected-(U2B-PB8-Pad45)
- U2 pad 6: /Power supply/GTX_1V0_EN -> /FPGA support/FPGA_PROG_B
- U4 pad D25: /FPGA/SFP_LED2 -> unconnected-(U4F-IO_L15N_T2_DQS_DOUT_CSO_B_14-PadD25)
- U4 pad J21: unconnected-(U4F-IO_L21P_T3_DQS_14-PadJ21) -> /FPGA/SFP_LED2
- U4 pad J23: /FPGA/FPGA_LED1 -> /FPGA/FPGA_LED0
- U4 pad K22: /FPGA/FPGA_LED3 -> /FPGA/FPGA_LED2
- U4 pad K23: /FPGA/FPGA_LED2 -> /FPGA/FPGA_LED1
- U4 pad L23: /FPGA/FPGA_LED0 -> /FPGA/FPGA_LED3
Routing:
- net /GND: track 1246.3 -> 1496.6 mm, vias 376 -> 480
- net /3V3_RAW: track 134.3 -> 250.5 mm, vias 13 -> 38
- net /1V2: track 130.1 -> 216.4 mm, vias 16 -> 31
- net /Power supply/5V0: track 0.00 -> 57.6 mm, vias 0 -> 28
- net /SoC support/SOC_RST_N: track 170.7 -> 121.2 mm
- net /FPGA support/GTX_1V0: track 17.9 -> 57.0 mm, vias 5 -> 17
- net /Power supply/SUPER_I2C2_SDA: track 0.00 -> 30.4 mm, vias 0 -> 2
- net /Power supply/SUPER_I2C2_SCL: track 0.00 -> 30.0 mm, vias 0 -> 2
- net /Power supply/SUPER_I2C_SCL: track 104.3 -> 130.3 mm, vias 1 -> 3
- net /FPGA/FLASH_DQ0: track 0.00 -> 25.0 mm
- net /FPGA/SFP_LED2: track 0.00 -> 24.4 mm, vias 0 -> 2
- net /FPGA/FLASH_CS_N: track 0.00 -> 24.3 mm, vias 0 -> 3
- net /FPGA/FLASH_DQ1: track 0.00 -> 23.9 mm
- net /Power supply/SUPER_JTAG_TMS: track 23.0 -> 45.5 mm, vias 1 -> 2
- net /Power supply/SOC_PWR_CPU_ON: track 61.6 -> 84.0 mm, vias 1 -> 2
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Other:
- board text added: "1V0"
- board text added: "1V2"
- board text added: "3V3_RAW"
- board text added: "5V0"
- board text added: "GTX_1V0"
- board text added: "I2C2"
- board text added: "SCL"
- board text added: "SDA"
